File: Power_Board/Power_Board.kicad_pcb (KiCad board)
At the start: 2 copper layers, 47.8 x 64.3 mm, 21 parts, among them J1 Conn_01x10_Female, J2 Conn_01x10_Female, J3 Conn_01x06_Male, J4 Screw_Terminal_01x02, J5 Screw_Terminal_01x02, J6 Conn_01x02_Male

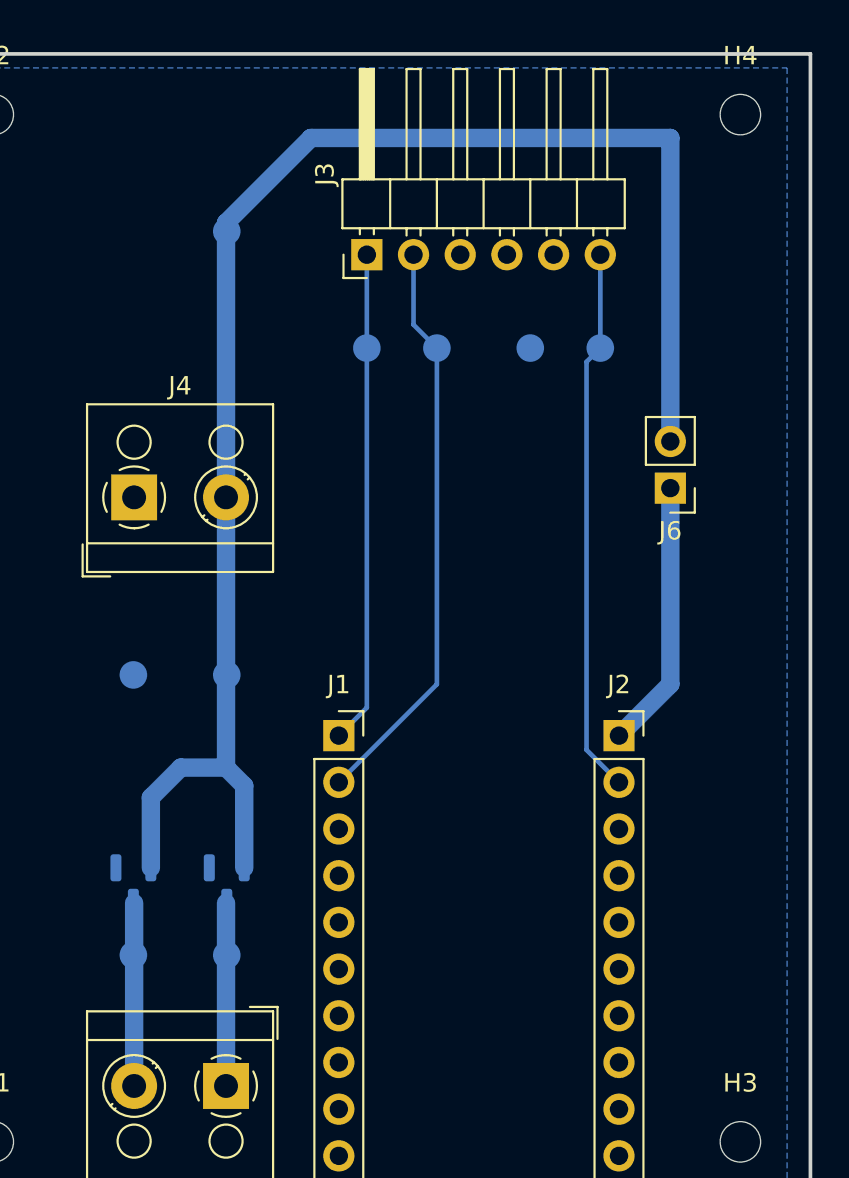
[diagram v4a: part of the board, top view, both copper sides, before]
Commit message: silkscreen added
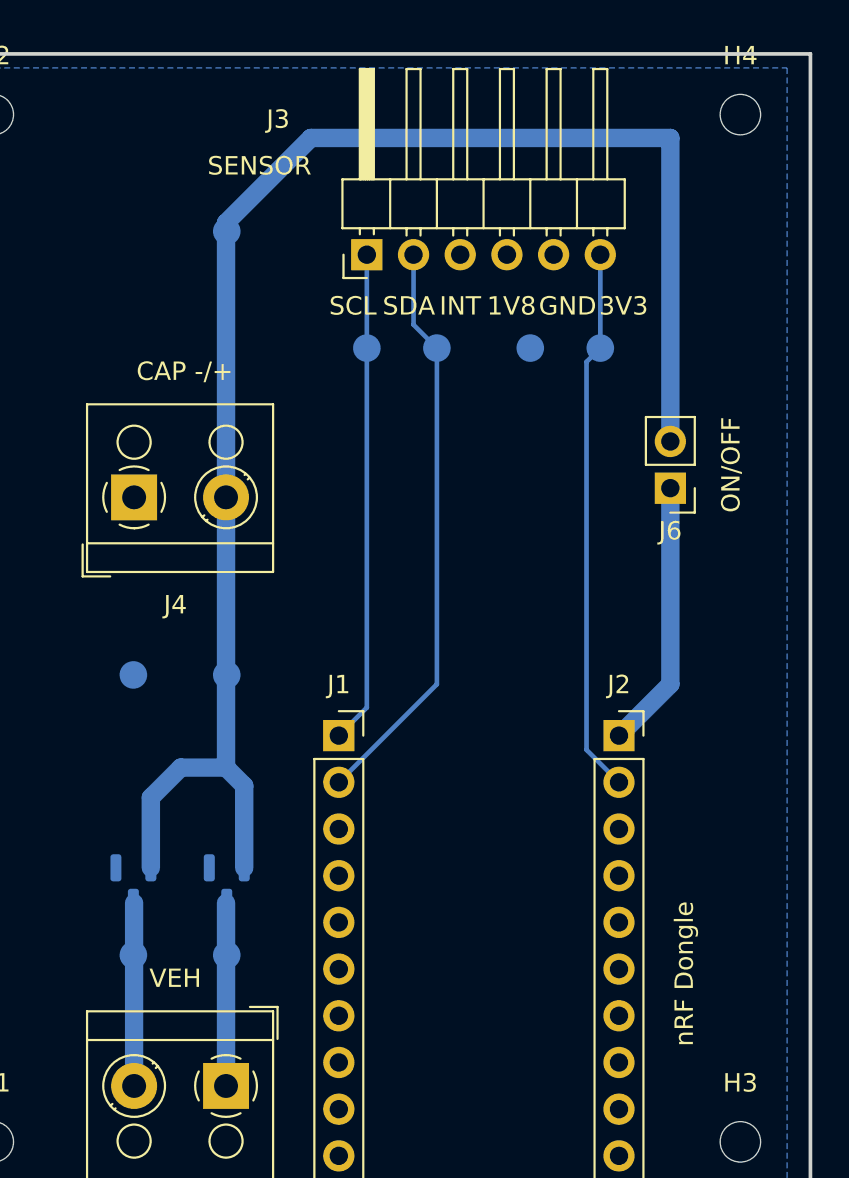
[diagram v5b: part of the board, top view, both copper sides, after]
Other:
- board text added: "1V8"
- board text added: "3V3"
- board text added: "C+"
- board text added: "CAP -/+"
- board text added: "GND"
- board text added: "INT"
- board text added: "ON/OFF"
- board text added: "SCL"
- board text added: "SDA"
- board text added: "SENSOR"
- board text added: "VDDOUT"
- board text added: "VEH"
- board text added: "VEH1"
- board text added: "VEH2"
- board text added: "VEH_OUT"
- board text added: "nRF Dongle"
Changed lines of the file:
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@@
     (property "Sheetname" "")
     (attr through_hole)
-    (fp_text reference "J3" (at 4.385 -2.27 90) (layer "F.SilkS")
+    (fp_text reference "J3" (at 7.366 -4.826 180) (layer "F.SilkS")
       (effects (font (size 1 1) (thickness 0.15)))
     )
@@
     (property "Sheetname" "")
     (attr through_hole)
-    (fp_text reference "J4" (at 2.5 -6.06) (layer "F.SilkS")
+    (fp_text reference "J4" (at 2.246 5.85) (layer "F.SilkS")
       (effects (font (size 1 1) (thickness 0.15)))
     )
@@
     (property "Sheetname" "")
     (attr exclude_from_pos_files)
-    (fp_text reference "TP7" (at 0 1.648 90) (layer "B.SilkS")
+    (fp_text reference "TP7" (at 0 -3.048 180) (layer "B.SilkS")
       (effects (font (size 1 1) (thickness 0.15)) (justify mirror))
     )
@@
     (property "Sheetname" "")
     (attr exclude_from_pos_files)
-    (fp_text reference "TP2" (at 0 1.648) (layer "B.SilkS")
+    (fp_text reference "TP2" (at -3.302 1.778) (layer "B.SilkS")
       (effects (font (size 1 1) (thickness 0.15)) (justify mirror))
     )
@@
     (property "Sheetname" "")
     (attr exclude_from_pos_files)
-    (fp_text reference "TP1" (at 0 1.648) (layer "B.SilkS")
+    (fp_text reference "TP1" (at 4.318 1.27) (layer "B.SilkS")
       (effects (font (size 1 1) (thickness 0.15)) (justify mirror))
     )
@@
     (property "Sheetname" "")
     (attr exclude_from_pos_files)
-    (fp_text reference "TP3" (at 0 1.648) (layer "B.SilkS")
+    (fp_text reference "TP3" (at -2.794 2.286) (layer "B.SilkS")
       (effects (font (size 1 1) (thickness 0.15)) (justify mirror))
     )
@@
     (property "Sheetname" "")
     (attr exclude_from_pos_files)
-    (fp_text reference "TP8" (at 0 1.648 90) (layer "B.SilkS")
+    (fp_text reference "TP8" (at 0 -3.302 180) (layer "B.SilkS")
       (effects (font (size 1 1) (thickness 0.15)) (justify mirror))
     )
@@
   (gr_rect (start 122.428 46.228) (end 170.18 110.49) (layer "Edge.Cuts") (width 0.2) (fill none))
   (gr_rect (start 159.512 111.572) (end 144.272 65.532) (layer "User.1") (width 0.15) (fill none))
+  (gr_text "GND" (at 154.94 64.516) (layer "B.SilkS")
+    (effects (font (size 1 1) (thickness 0.15)) (justify mirror))
+  )
+  (gr_text "VEH2" (at 141.732 95.504) (layer "B.SilkS")
+    (effects (font (size 1 1) (thickness 0.15)) (justify mirror))
+  )
+  (gr_text "GND" (at 130.048 82.296) (layer "B.SilkS")
+    (effects (font (size 1 1) (thickness 0.15)) (justify mirror))
+  )
+  (gr_text "SDA" (at 149.86 64.516) (layer "B.SilkS")
+    (effects (font (size 1 1) (thickness 0.15)) (justify mirror))
+  )
+  (gr_text "SCL" (at 145.796 64.516) (layer "B.SilkS")
+    (effects (font (size 1 1) (thickness 0.15)) (justify mirror))
+  )
+  (gr_text "VEH_OUT" (at 142.748 79.248) (layer "B.SilkS")
+    (effects (font (size 1 1) (thickness 0.15)) (justify mirror))
+  )
+  (gr_text "VDDOUT" (at 160.528 64.516) (layer "B.SilkS")
+    (effects (font (size 1 1) (thickness 0.15)) (justify mirror))
+  )
+  (gr_text "VEH1" (at 129.032 96.012) (layer "B.SilkS")
+    (effects (font (size 1 1) (thickness 0.15)) (justify mirror))
+  )
+  (gr_text "C+" (at 135.128 57.404) (layer "B.SilkS")
+    (effects (font (size 1 1) (thickness 0.15)) (justify mirror))
+  )
+  (gr_text "3V3" (at 160.02 59.944) (layer "F.SilkS")
+    (effects (font (size 1 1) (thickness 0.15)))
+  )
+  (gr_text "VEH" (at 135.636 96.52) (layer "F.SilkS")
+    (effects (font (size 1 1) (thickness 0.15)))
+  )
+  (gr_text "ON/OFF" (at 165.862 68.58 90) (layer "F.SilkS")
+    (effects (font (size 1 1) (thickness 0.15)))
+  )
+  (gr_text "GND" (at 156.972 59.944) (layer "F.SilkS")
+    (effects (font (size 1 1) (thickness 0.15)))
+  )
+  (gr_text "SDA" (at 148.336 59.944) (layer "F.SilkS")
+    (effects (font (size 1 1) (thickness 0.15)))
+  )
+  (gr_text "SENSOR" (at 140.208 52.324) (layer "F.SilkS")
+    (effects (font (size 1 1) (thickness 0.15)))
+  )
+  (gr_text "INT\n" (at 151.13 59.944) (layer "F.SilkS")
+    (effects (font (size 1 1) (thickness 0.15)))
+  )
+  (gr_text "nRF Dongle\n" (at 163.322 96.266 90) (layer "F.SilkS")
+    (effects (font (size 1 1) (thickness 0.15)))
+  )
+  (gr_text "CAP -/+" (at 136.144 63.5) (layer "F.SilkS")
+    (effects (font (size 1 1) (thickness 0.15)))
+  )
+  (gr_text "SCL\n" (at 145.288 59.944) (layer "F.SilkS")
+    (effects (font (size 1 1) (thickness 0.15)))
+  )
+  (gr_text "1V8\n" (at 153.924 59.944) (layer "F.SilkS")
+    (effects (font (size 1 1) (thickness 0.15)))
+  )
   (segment (start 162.56 80.518) (end 159.766 83.312) (width 1) (layer "B.Cu") (net 2))
   (segment (start 162.56 69.85) (end 162.56 80.518) (width 1) (layer "B.Cu") (net 2))

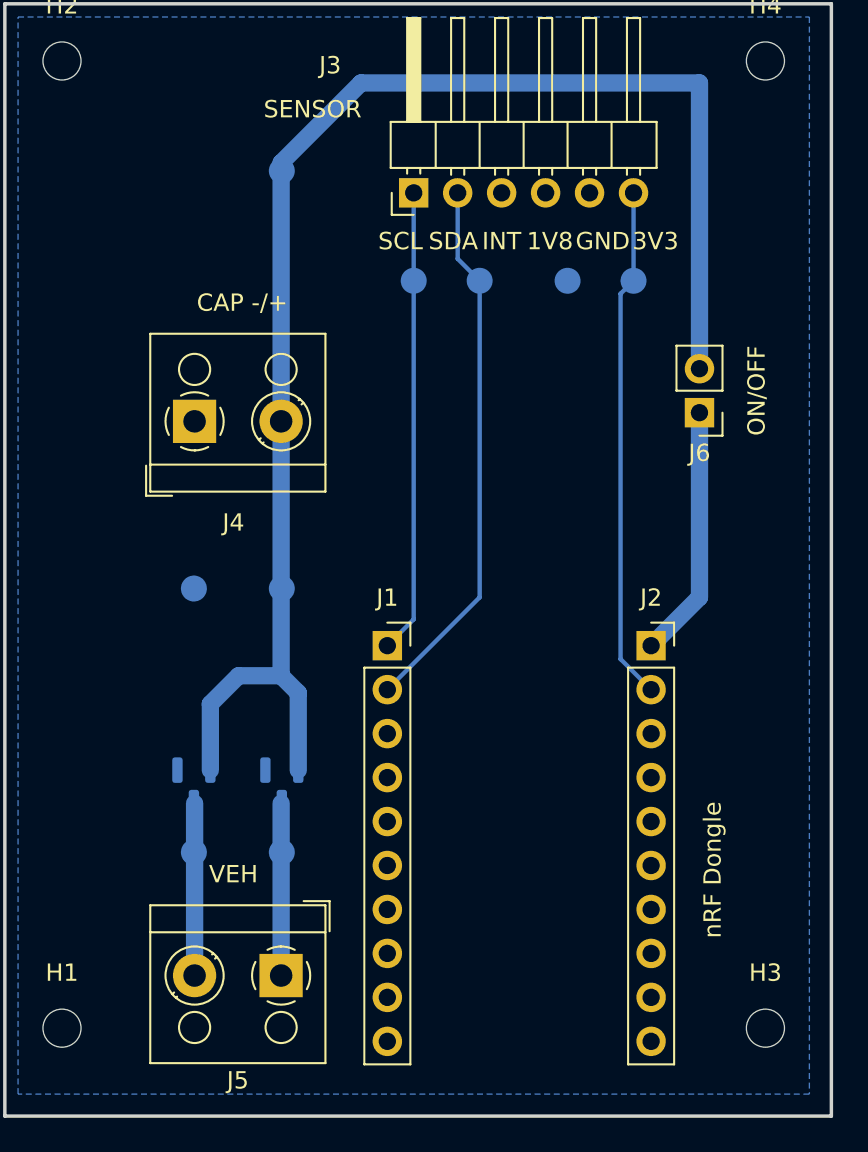
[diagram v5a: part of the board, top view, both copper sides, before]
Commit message: Thicker traces, swaped text
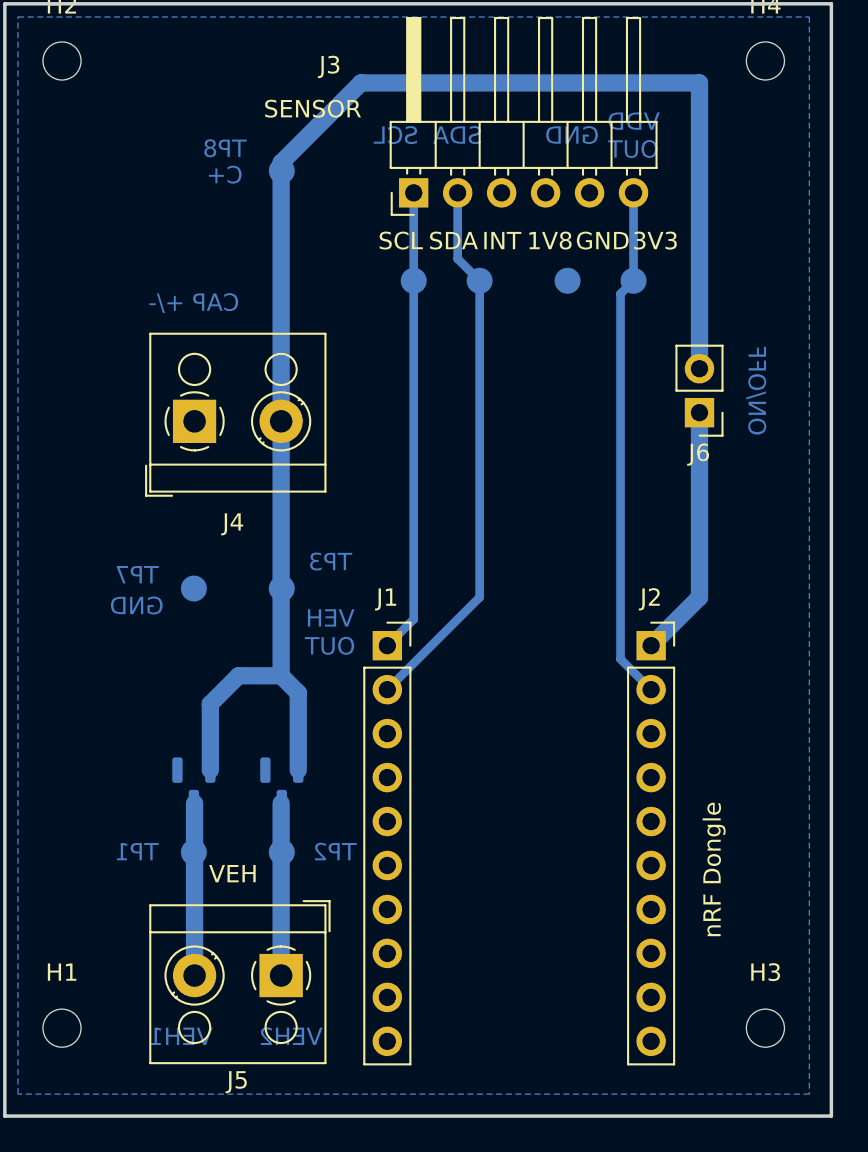
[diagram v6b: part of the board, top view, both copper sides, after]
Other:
- board text added: "CAP +/-"
- board text added: "VDD OUT"
- board text added: "VEH OUT"
- board text removed: "CAP -/+"
- board text removed: "VDDOUT"
- board text removed: "VEH_OUT"
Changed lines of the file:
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@@
     (pad_to_mask_clearance 0)
     (pcbplotparams
-      (layerselection 0x00010fc_ffffffff)
+      (layerselection 0x0001000_fffffffe)
       (disableapertmacros false)
       (usegerberextensions false)
@@
       (outputformat 1)
       (mirror false)
-      (drillshape 1)
+      (drillshape 0)
       (scaleselection 1)
       (outputdirectory "")
@@
     (property "Sheetname" "")
     (attr exclude_from_pos_files)
-    (fp_text reference "TP7" (at 0 -3.048 180) (layer "B.SilkS")
+    (fp_text reference "TP7" (at 0.762 -3.302 180) (layer "B.Cu")
       (effects (font (size 1 1) (thickness 0.15)) (justify mirror))
     )
@@
     (property "Sheetname" "")
     (attr exclude_from_pos_files)
-    (fp_text reference "TP2" (at -3.302 1.778) (layer "B.SilkS")
+    (fp_text reference "TP2" (at -3.048 0) (layer "B.Cu")
       (effects (font (size 1 1) (thickness 0.15)) (justify mirror))
     )
@@
     (property "Sheetname" "")
     (attr exclude_from_pos_files)
-    (fp_text reference "TP1" (at 4.318 1.27) (layer "B.SilkS")
+    (fp_text reference "TP1" (at 3.302 0) (layer "B.Cu")
       (effects (font (size 1 1) (thickness 0.15)) (justify mirror))
     )
@@
     (property "Sheetname" "")
     (attr exclude_from_pos_files)
-    (fp_text reference "TP3" (at -2.794 2.286) (layer "B.SilkS")
+    (fp_text reference "TP3" (at -2.794 1.524) (layer "B.Cu")
       (effects (font (size 1 1) (thickness 0.15)) (justify mirror))
     )
@@
     (property "Sheetname" "")
     (attr exclude_from_pos_files)
-    (fp_text reference "TP8" (at 0 -3.302 180) (layer "B.SilkS")
+    (fp_text reference "TP8" (at 1.27 -3.302 180) (layer "B.Cu")
       (effects (font (size 1 1) (thickness 0.15)) (justify mirror))
     )
@@
   (gr_rect (start 122.428 46.228) (end 170.18 110.49) (layer "Edge.Cuts") (width 0.2) (fill none))
   (gr_rect (start 159.512 111.572) (end 144.272 65.532) (layer "User.1") (width 0.15) (fill none))
-  (gr_text "GND" (at 154.94 64.516) (layer "B.SilkS")
-    (effects (font (size 1 1) (thickness 0.15)) (justify mirror))
-  )
-  (gr_text "VEH2" (at 141.732 95.504) (layer "B.SilkS")
-    (effects (font (size 1 1) (thickness 0.15)) (justify mirror))
-  )
-  (gr_text "GND" (at 130.048 82.296) (layer "B.SilkS")
-    (effects (font (size 1 1) (thickness 0.15)) (justify mirror))
-  )
-  (gr_text "SDA" (at 149.86 64.516) (layer "B.SilkS")
-    (effects (font (size 1 1) (thickness 0.15)) (justify mirror))
-  )
-  (gr_text "SCL" (at 145.796 64.516) (layer "B.SilkS")
-    (effects (font (size 1 1) (thickness 0.15)) (justify mirror))
-  )
-  (gr_text "VEH_OUT" (at 142.748 79.248) (layer "B.SilkS")
-    (effects (font (size 1 1) (thickness 0.15)) (justify mirror))
-  )
-  (gr_text "VDDOUT" (at 160.528 64.516) (layer "B.SilkS")
-    (effects (font (size 1 1) (thickness 0.15)) (justify mirror))
-  )
-  (gr_text "VEH1" (at 129.032 96.012) (layer "B.SilkS")
-    (effects (font (size 1 1) (thickness 0.15)) (justify mirror))
-  )
-  (gr_text "C+" (at 135.128 57.404) (layer "B.SilkS")
+  (gr_text "GND" (at 155.194 53.848) (layer "B.Cu")
+    (effects (font (size 1 1) (thickness 0.15)) (justify mirror))
+  )
+  (gr_text "VEH2" (at 138.938 105.918) (layer "B.Cu")
+    (effects (font (size 1 1) (thickness 0.15)) (justify mirror))
+  )
+  (gr_text "ON/OFF" (at 165.862 68.58 -90) (layer "B.Cu")
+    (effects (font (size 1 1) (thickness 0.15)) (justify mirror))
+  )
+  (gr_text "GND" (at 130.048 81.026) (layer "B.Cu")
+    (effects (font (size 1 1) (thickness 0.15)) (justify mirror))
+  )
+  (gr_text "SDA" (at 148.59 53.848) (layer "B.Cu")
+    (effects (font (size 1 1) (thickness 0.15)) (justify mirror))
+  )
+  (gr_text "SCL" (at 145.034 53.848) (layer "B.Cu")
+    (effects (font (size 1 1) (thickness 0.15)) (justify mirror))
+  )
+  (gr_text "VEH\nOUT" (at 141.224 82.55) (layer "B.Cu")
+    (effects (font (size 1 1) (thickness 0.15)) (justify mirror))
+  )
+  (gr_text "CAP +/-" (at 133.35 63.5) (layer "B.Cu")
+    (effects (font (size 1 1) (thickness 0.15)) (justify mirror))
+  )
+  (gr_text "VDD\nOUT" (at 158.75 53.848) (layer "B.Cu")
+    (effects (font (size 1 1) (thickness 0.15)) (justify mirror))
+  )
+  (gr_text "VEH1" (at 132.588 105.918) (layer "B.Cu")
+    (effects (font (size 1 1) (thickness 0.15)) (justify mirror))
+  )
+  (gr_text "C+" (at 135.128 56.134) (layer "B.Cu")
     (effects (font (size 1 1) (thickness 0.15)) (justify mirror))
   )
@@
     (effects (font (size 1 1) (thickness 0.15)))
   )
-  (gr_text "ON/OFF" (at 165.862 68.58 90) (layer "F.SilkS")
-    (effects (font (size 1 1) (thickness 0.15)))
-  )
   (gr_text "GND" (at 156.972 59.944) (layer "F.SilkS")
     (effects (font (size 1 1) (thickness 0.15)))
@@
   )
   (gr_text "nRF Dongle\n" (at 163.322 96.266 90) (layer "F.SilkS")
-    (effects (font (size 1 1) (thickness 0.15)))
-  )
-  (gr_text "CAP -/+" (at 136.144 63.5) (layer "F.SilkS")
     (effects (font (size 1 1) (thickness 0.15)))
   )
@@
   (segment (start 138.39 102.37) (end 138.39 92.4175) (width 1) (layer "B.Cu") (net 4))
   (segment (start 138.39 92.4175) (end 138.43 92.3775) (width 0.254) (layer "B.Cu") (net 4))
-  (segment (start 146.05 81.788) (end 144.526 83.312) (width 0.254) (layer "B.Cu") (net 5))
-  (segment (start 146.05 62.23) (end 146.05 81.788) (width 0.254) (layer "B.Cu") (net 5))
-  (segment (start 146.05 57.15) (end 146.05 62.23) (width 0.254) (layer "B.Cu") (net 5))
-  (segment (start 149.86 80.518) (end 149.86 62.23) (width 0.254) (layer "B.Cu") (net 6))
-  (segment (start 148.59 57.15) (end 148.59 60.96) (width 0.254) (layer "B.Cu") (net 6))
-  (segment (start 148.59 60.96) (end 149.86 62.23) (width 0.254) (layer "B.Cu") (net 6))
-  (segment (start 144.526 85.852) (end 149.86 80.518) (width 0.254) (layer "B.Cu") (net 6))
+  (segment (start 146.05 81.788) (end 144.526 83.312) (width 0.5) (layer "B.Cu") (net 5))
+  (segment (start 146.05 62.23) (end 146.05 81.788) (width 0.5) (layer "B.Cu") (net 5))
+  (segment (start 146.05 57.15) (end 146.05 62.23) (width 0.5) (layer "B.Cu") (net 5))
+  (segment (start 149.86 80.518) (end 149.86 62.23) (width 0.5) (layer "B.Cu") (net 6))
+  (segment (start 148.59 57.15) (end 148.59 60.96) (width 0.5) (layer "B.Cu") (net 6))
+  (segment (start 148.59 60.96) (end 149.86 62.23) (width 0.5) (layer "B.Cu") (net 6))
+  (segment (start 144.526 85.852) (end 149.86 80.518) (width 0.5) (layer "B.Cu") (net 6))
   (segment (start 138.39 70.35) (end 138.39 55.416576) (width 1) (layer "B.Cu") (net 22))
   (segment (start 135.93 85.05) (end 138.39 85.05) (width 1) (layer "B.Cu") (net 22))
@@
   (segment (start 138.39 55.416576) (end 143.006576 50.8) (width 1) (layer "B.Cu") (net 22))
   (segment (start 138.39 85.05) (end 138.39 70.35) (width 1) (layer "B.Cu") (net 22))
-  (segment (start 158 84.086) (end 159.766 85.852) (width 0.254) (layer "B.Cu") (net 23))
-  (segment (start 158 62.98) (end 158 84.086) (width 0.254) (layer "B.Cu") (net 23))
-  (segment (start 158.75 62.23) (end 158.75 57.15) (width 0.254) (layer "B.Cu") (net 23))
-  (segment (start 158.75 62.23) (end 158 62.98) (width 0.254) (layer "B.Cu") (net 23))
+  (segment (start 158 84.086) (end 159.766 85.852) (width 0.5) (layer "B.Cu") (net 23))
+  (segment (start 158 62.98) (end 158 84.086) (width 0.5) (layer "B.Cu") (net 23))
+  (segment (start 158.75 62.23) (end 158.75 57.15) (width 0.5) (layer "B.Cu") (net 23))
+  (segment (start 158.75 62.23) (end 158 62.98) (width 0.5) (layer "B.Cu") (net 23))
   (zone (net 1) (net_name "GND") (layer "B.Cu") (hatch edge 0.508)
     (connect_pads (clearance 0.508))
     (min_thickness 0.254) (filled_areas_thickness no)
-    (fill yes (thermal_gap 0.508) (thermal_bridge_width 0.508))
+    (fill yes (thermal_gap 0.508) (thermal_bridge_width 0.508) (island_removal_mode 1) (island_area_min 0))
     (polygon
       (pts
